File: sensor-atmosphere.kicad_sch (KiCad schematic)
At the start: 16 parts, among them J4 STEMMA_I2C_QT, J5 Conn_01x07, J6 STEMMA_I2C_QT, Q2 BSS138BKS,115, U6 XC6210B332MR-G, U7 BME688

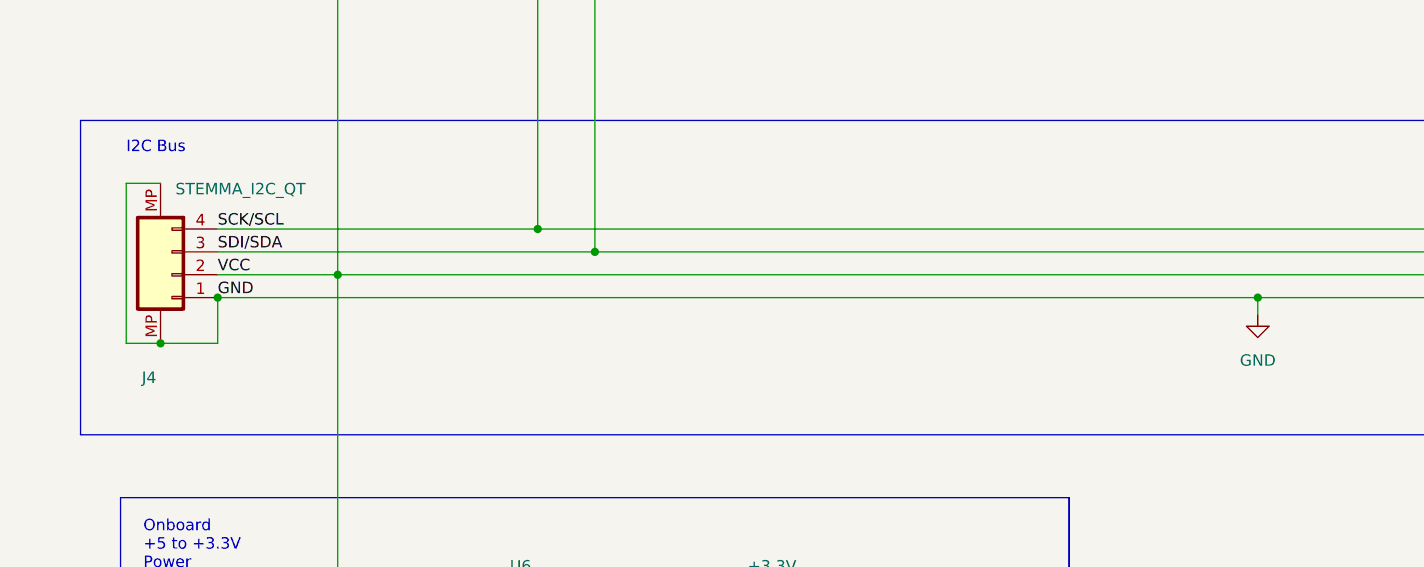
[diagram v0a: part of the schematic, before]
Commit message: Adding I2C bus to circuit
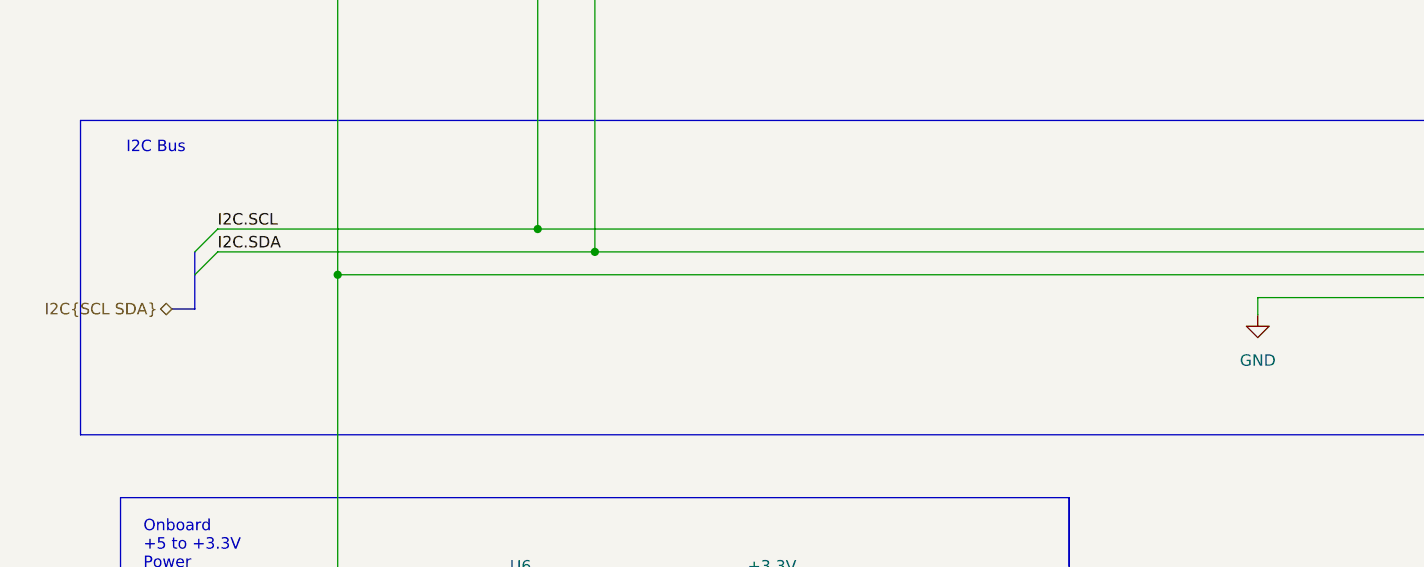
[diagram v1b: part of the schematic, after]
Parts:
- removed J4: STEMMA_I2C_QT, Connector_JST:JST_SH_SM04B-SRSS-TB_1x04-1MP_P1.00mm_Horizontal, symbol Lab_4:STEMMA_I2C_QT
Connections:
- net SCK/SCL renamed I2C.SCL
- net SDI/SDA renamed I2C.SDA
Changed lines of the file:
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@@
-	)
-	(junction
-		(at 40.64 119.38)
-		(diameter 0)
-		(color 0 0 0 0)
 	)
 	(junction
@@
 	)
 	(junction
-		(at 156.21 119.38)
-		(diameter 0)
-		(color 0 0 0 0)
-	)
-	(junction
 		(at 143.51 33.655)
 		(diameter 0)
@@
 	(junction
 		(at 66.675 154.305)
-		(diameter 0)
-		(color 0 0 0 0)
-	)
-	(junction
-		(at 34.29 124.46)
 		(diameter 0)
 		(color 0 0 0 0)
@@
 		(at 81.915 156.845)
 	)
+	(bus_entry
+		(at 40.64 114.3)
+		(size -2.54 2.54)
+		(stroke
+			(width 0)
+			(type default)
+		)
+	)
+	(bus_entry
+		(at 40.64 111.76)
+		(size -2.54 2.54)
+		(stroke
+			(width 0)
+			(type default)
+		)
+	)
 	(wire
 		(pts
@@
 		)
 	)
-	(wire
-		(pts
-			(xy 30.48 124.46) (xy 34.29 124.46)
-		)
-		(stroke
-			(width 0)
-			(type default)
-		)
-	)
 	(polyline
 		(pts
@@
 	(wire
 		(pts
-			(xy 30.48 106.68) (xy 34.29 106.68)
-		)
-		(stroke
-			(width 0)
-			(type default)
-		)
-	)
-	(wire
-		(pts
-			(xy 40.64 119.38) (xy 156.21 119.38)
-		)
-		(stroke
-			(width 0)
-			(type default)
-		)
-	)
-	(wire
-		(pts
 			(xy 102.235 164.465) (xy 90.17 164.465)
 		)
@@
 	(wire
 		(pts
-			(xy 34.29 124.46) (xy 40.64 124.46)
-		)
-		(stroke
-			(width 0)
-			(type default)
-		)
-	)
-	(wire
-		(pts
 			(xy 59.69 53.34) (xy 59.69 59.055)
 		)
@@
 		)
 	)
-	(wire
-		(pts
-			(xy 40.64 116.84) (xy 53.975 116.84)
+	(bus
+		(pts
+			(xy 35.56 120.65) (xy 38.1 120.65)
 		)
 		(stroke
@@
 	(wire
 		(pts
-			(xy 30.48 106.68) (xy 30.48 124.46)
-		)
-		(stroke
-			(width 0)
-			(type default)
-		)
-	)
-	(wire
-		(pts
 			(xy 238.76 75.565) (xy 236.22 75.565)
 		)
@@
 		)
 	)
+	(bus
+		(pts
+			(xy 38.1 114.3) (xy 38.1 116.84)
+		)
+		(stroke
+			(width 0)
+			(type default)
+		)
+	)
 	(wire
 		(pts
@@
 		)
 	)
+	(bus
+		(pts
+			(xy 38.1 116.84) (xy 38.1 120.65)
+		)
+		(stroke
+			(width 0)
+			(type default)
+		)
+	)
 	(wire
 		(pts
@@
 		(pts
 			(xy 113.03 46.355) (xy 113.03 62.865)
-		)
-		(stroke
-			(width 0)
-			(type default)
-		)
-	)
-	(wire
-		(pts
-			(xy 40.64 119.38) (xy 40.64 124.46)
 		)
 		(stroke
@@
 		)
 	)
-	(label "SCK{slash}SCL"
+	(label "I2C.SCL"
 		(at 40.64 111.76 0)
 		(fields_autoplaced yes)
@@
 		)
 	)
-	(label "VCC"
-		(at 40.64 116.84 0)
-		(fields_autoplaced yes)
-		(effects
-			(font
-				(size 1.27 1.27)
-			)
-			(justify left bottom)
-		)
-	)
-	(label "GND"
-		(at 40.64 119.38 0)
-		(fields_autoplaced yes)
-		(effects
-			(font
-				(size 1.27 1.27)
-			)
-			(justify left bottom)
-		)
-	)
 	(label "SDI_3V"
 		(at 215.9 62.865 0)
@@
 		)
 	)
-	(label "SDI{slash}SDA"
+	(label "I2C.SDA"
 		(at 40.64 114.3 0)
 		(fields_autoplaced yes)
@@
 			)
 			(justify left bottom)
+		)
+	)
+	(hierarchical_label "I2C{SCL SDA}"
+		(shape bidirectional)
+		(at 35.56 120.65 180)
+		(fields_autoplaced yes)
+		(effects
+			(font
+				(size 1.27 1.27)
+			)
+			(justify right)
 		)
 	)
@@
 					(unit 1)
 				)
-			)
-		)
-	)
-	(symbol
-		(lib_name "STEMMA_I2C_QT_1")
-		(lib_id "Lab_4:STEMMA_I2C_QT")
-		(at 35.56 116.84 180)
-		(unit 1)
-		(exclude_from_sim no)
-		(in_bom yes)
-		(on_board yes)
-		(dnp no)
-		(property "Reference" "J4"
-			(at 33.02 128.27 0)
-			(effects
-				(font
-					(size 1.27 1.27)
-				)
-			)
-		)
-		(property "Value" "STEMMA_I2C_QT"
-			(at 43.18 107.315 0)
-			(effects
-				(font
-					(size 1.27 1.27)
-				)
-			)
-		)
-		(property "Footprint" "Connector_JST:JST_SH_SM04B-SRSS-TB_1x04-1MP_P1.00mm_Horizontal"
-			(at 35.56 116.84 0)
-			(effects
-				(font
-					(size 1.27 1.27)
-				)
-				(hide yes)
-			)
-		)
-		(property "Datasheet" "https://www.jst-mfg.com/product/pdf/eng/eSH.pdf"
-			(at 35.56 116.84 0)
-			(effects
-				(font
-					(size 1.27 1.27)
-				)
-				(hide yes)
-			)
-		)
-		(property "Description" "Connector Header Surface Mount, Right Angle 4 position 0.039\" (1.00mm)"
-			(at 35.56 116.84 0)
-			(effects
-				(font
-					(size 1.27 1.27)
-				)
-				(hide yes)
-			)
-		)
-		(property "Vendor" "DigiKey"
-			(at 35.56 116.84 0)
-			(effects
-				(font
-					(size 1.27 1.27)
-				)
-				(hide yes)
-			)
-		)
-		(property "Vendor P/N" "455-1804-1-ND "
-			(at 35.56 116.84 0)
-			(effects
-				(font
-					(size 1.27 1.27)
-				)
-				(hide yes)
-			)
-		)
-		(property "Mfr" "JST Sales America Inc."
-			(at 35.56 116.84 0)
-			(effects
-				(font
-					(size 1.27 1.27)
-				)
-				(hide yes)
-			)
-		)
-		(property "Mfr P/N" "SM04B-SRSS-TB"
-			(at 35.56 116.84 0)
-			(effects
-				(font
-					(size 1.27 1.27)
-				)
-				(hide yes)
-			)
-		)
-		(property "Supplier 1" ""
-			(at 35.56 116.84 0)
-			(effects
-				(font
-					(size 1.27 1.27)
-				)
-				(hide yes)
-			)
-		)
-		(property "Supplier 1 P/N" ""
-			(at 35.56 116.84 0)
-			(effects
-				(font
-					(size 1.27 1.27)
-				)
-				(hide yes)
-			)
-		)
-		(property "Supplier 2" ""
-			(at 35.56 116.84 0)
-			(effects
-				(font
-					(size 1.27 1.27)
-				)
-				(hide yes)
-			)
-		)
-		(property "Supplier 2 P/N" ""
-			(at 35.56 116.84 0)
-			(effects
-				(font
-					(size 1.27 1.27)
-				)
-				(hide yes)
-			)
-		)
-		(pin "MP"
-		)
-		(pin "MP"
-		)
-		(pin "1"
-		)
-		(pin "2"
-		)
-		(pin "3"
-		)
-		(pin "4"
-		)
-		(instances
-			(project "roamer"
-				(path "/1c59de6a-87fe-4223-8898-4b0383164a31/10ed27ff-b06a-41c0-90a7-6ef09f5e2ce1"
-					(reference "J4")
-					(unit 1)
-				)

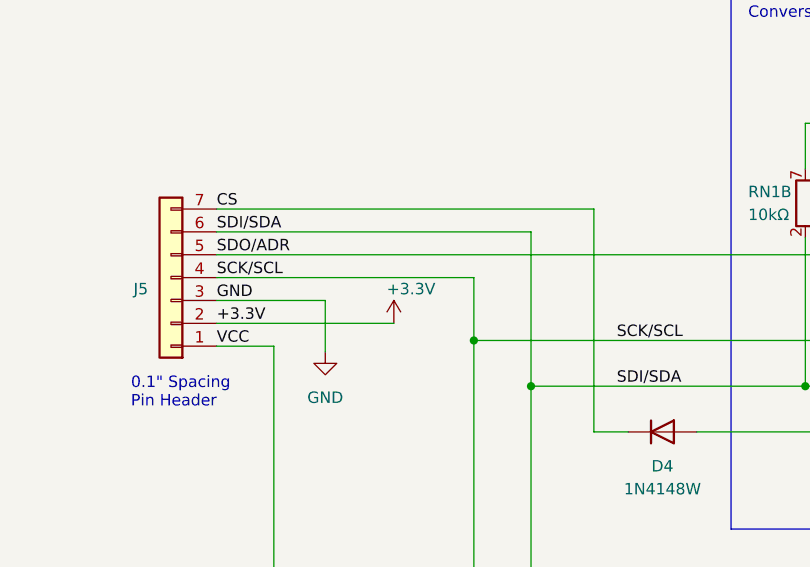
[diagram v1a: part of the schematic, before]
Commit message: Adding symbols information
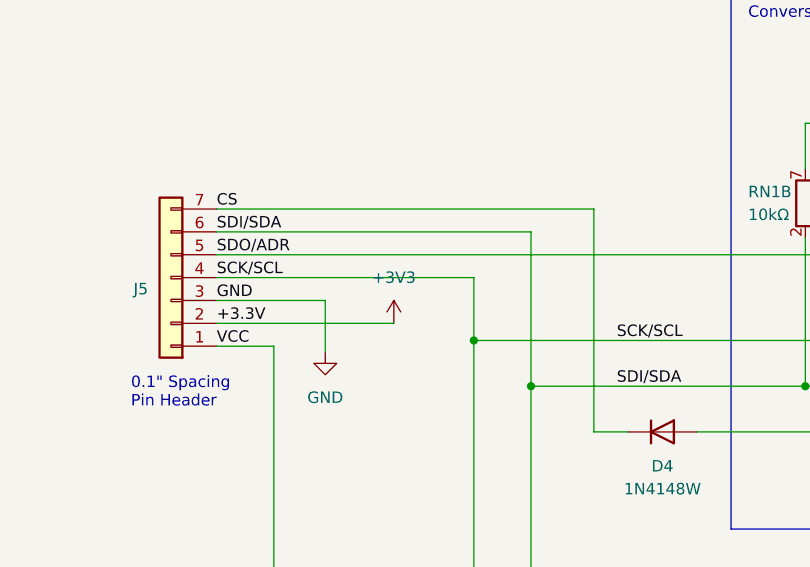
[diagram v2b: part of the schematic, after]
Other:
- company: (none) -> catbranchman
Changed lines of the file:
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@@
 	(generator_version "8.0")
 	(paper "A4")
+	(title_block
+		(company "catbranchman")
+		(comment 1 "Electrical Engineering Department")
+		(comment 2 "EE 156 / Stanford University")
+		(comment 3 "Flight Club, W6YX, Endurance")
+	)
 	(junction
 		(at 238.76 45.085)
@@
 	)
 	(symbol
-		(lib_name "+3.3V_3")
-		(lib_id "power:+3.3V")
-		(at 67.31 55.88 0)
-		(unit 1)
-		(exclude_from_sim no)
-		(in_bom yes)
-		(on_board yes)
-		(dnp no)
-		(property "Reference" "#PWR042"
-			(at 67.31 59.69 0)
-			(effects
-				(font
-					(size 1.27 1.27)
-				)
-				(hide yes)
-			)
-		)
-		(property "Value" "+3.3V"
-			(at 69.215 52.07 0)
-			(effects
-				(font
-					(size 1.27 1.27)
-				)
-			)
-		)
-		(property "Footprint" ""
-			(at 67.31 55.88 0)
-			(effects
-				(font
-					(size 1.27 1.27)
-				)
-				(hide yes)
-			)
-		)
-		(property "Datasheet" ""
-			(at 67.31 55.88 0)
-			(effects
-				(font
-					(size 1.27 1.27)
-				)
-				(hide yes)
-			)
-		)
-		(property "Description" ""
-			(at 67.31 55.88 0)
-			(effects
-				(font
-					(size 1.27 1.27)
-				)
-				(hide yes)
-			)
-		)
-		(property "Mfr" ""
-			(at 67.31 55.88 0)
-			(effects
-				(font
-					(size 1.27 1.27)
-				)
-				(hide yes)
-			)
-		)
-		(property "Mfr P/N" ""
-			(at 67.31 55.88 0)
-			(effects
-				(font
-					(size 1.27 1.27)
-				)
-				(hide yes)
-			)
-		)
-		(property "Supplier 1" ""
-			(at 67.31 55.88 0)
-			(effects
-				(font
-					(size 1.27 1.27)
-				)
-				(hide yes)
-			)
-		)
-		(property "Supplier 1 P/N" ""
-			(at 67.31 55.88 0)
-			(effects
-				(font
-					(size 1.27 1.27)
-				)
-				(hide yes)
-			)
-		)
-		(property "Supplier 2" ""
-			(at 67.31 55.88 0)
-			(effects
-				(font
-					(size 1.27 1.27)
-				)
-				(hide yes)
-			)
-		)
-		(property "Supplier 2 P/N" ""
-			(at 67.31 55.88 0)
-			(effects
-				(font
-					(size 1.27 1.27)
-				)
-				(hide yes)
-			)
-		)
-		(pin "1"
-		)
-		(instances
-			(project "roamer"
-				(path "/1c59de6a-87fe-4223-8898-4b0383164a31/10ed27ff-b06a-41c0-90a7-6ef09f5e2ce1"
-					(reference "#PWR042")
-					(unit 1)
-				)
-			)
-		)
-	)
-	(symbol
 		(lib_name "GND_6")
 		(lib_id "power:GND")
@@
 				)
 			)
+		)
+	)
+	(symbol
+		(lib_id "power:+3V3")
+		(at 67.31 55.88 0)
+		(unit 1)
+		(exclude_from_sim no)
+		(in_bom yes)
+		(on_board yes)
+		(dnp no)
+		(fields_autoplaced yes)
+		(property "Reference" "#PWR042"
+			(at 67.31 59.69 0)
+			(effects
+				(font
+					(size 1.27 1.27)
+				)
+				(hide yes)
+			)
+		)
+		(property "Value" "+3V3"
+			(at 67.31 50.8 0)
+			(effects
+				(font
+					(size 1.27 1.27)
+				)
+			)
+		)
+		(property "Footprint" ""
+			(at 67.31 55.88 0)
+			(effects
+				(font
+					(size 1.27 1.27)
+				)
+				(hide yes)
+			)
+		)
+		(property "Datasheet" ""
+			(at 67.31 55.88 0)
+			(effects
+				(font
+					(size 1.27 1.27)
+				)
+				(hide yes)
+			)
+		)
+		(property "Description" "Power symbol creates a global label with name \"+3V3\""
+			(at 67.31 55.88 0)
+			(effects
+				(font
+					(size 1.27 1.27)
+				)
+				(hide yes)
+			)
+		)
+		(pin "1"
+		)
+		(instances
+			(project "roamer"
+				(path "/1c59de6a-87fe-4223-8898-4b0383164a31/10ed27ff-b06a-41c0-90a7-6ef09f5e2ce1"
+					(reference "#PWR042")
+					(unit 1)
+				)
+			)

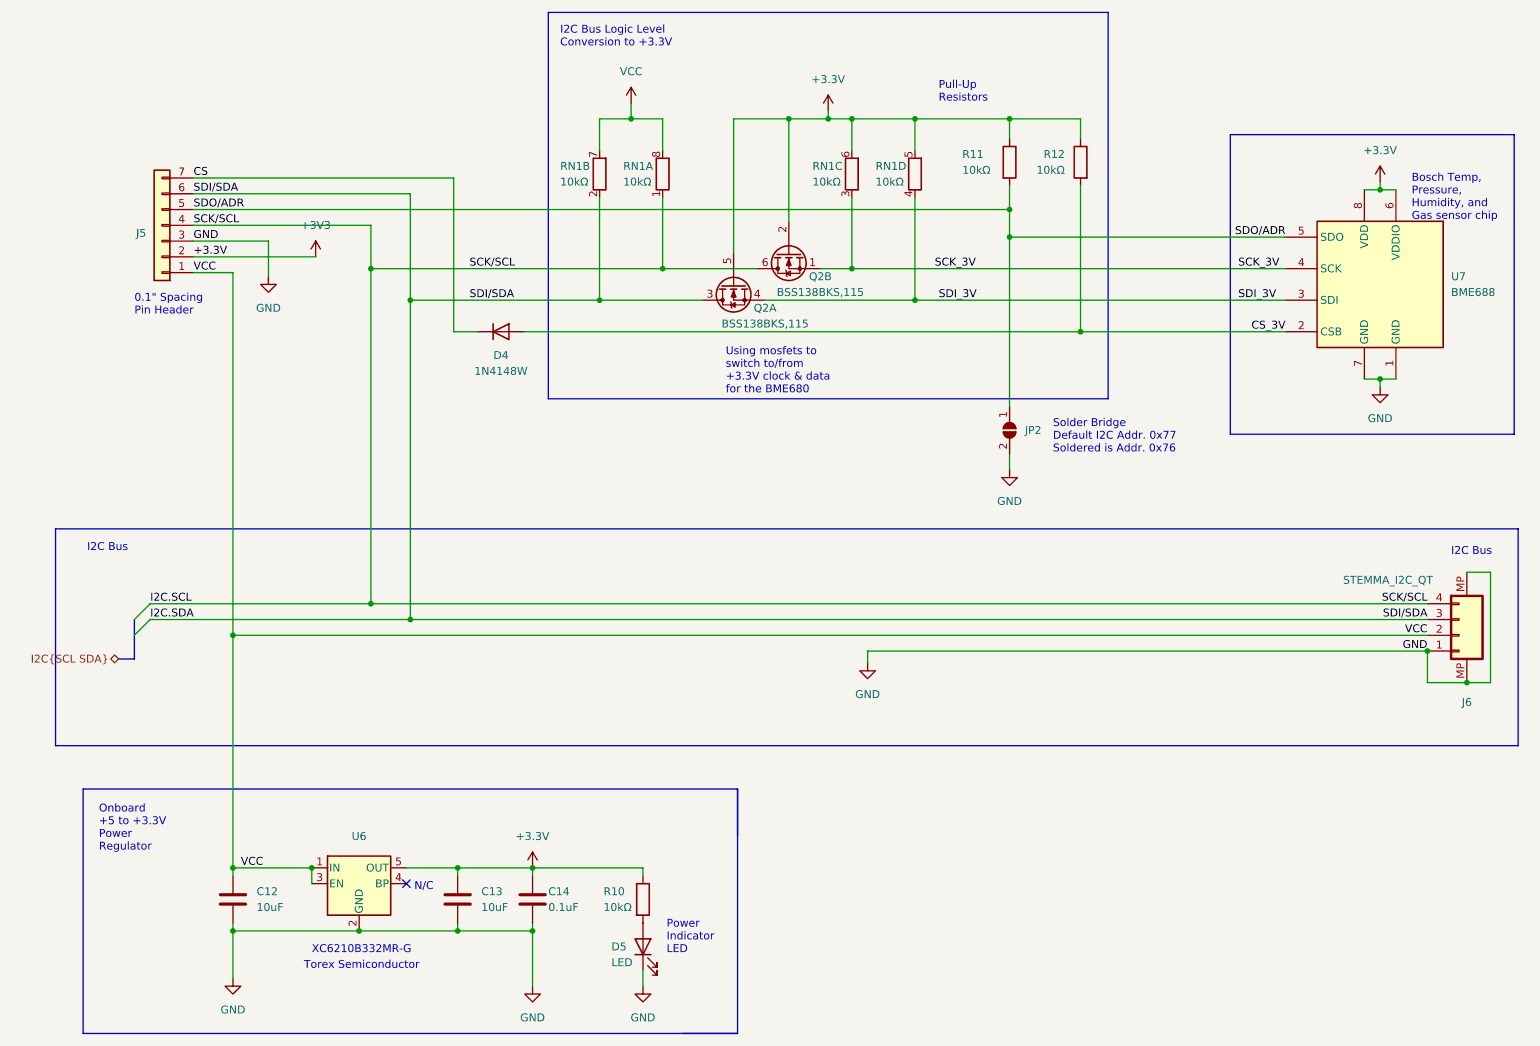
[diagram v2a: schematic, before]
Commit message: Adding rest of schematic
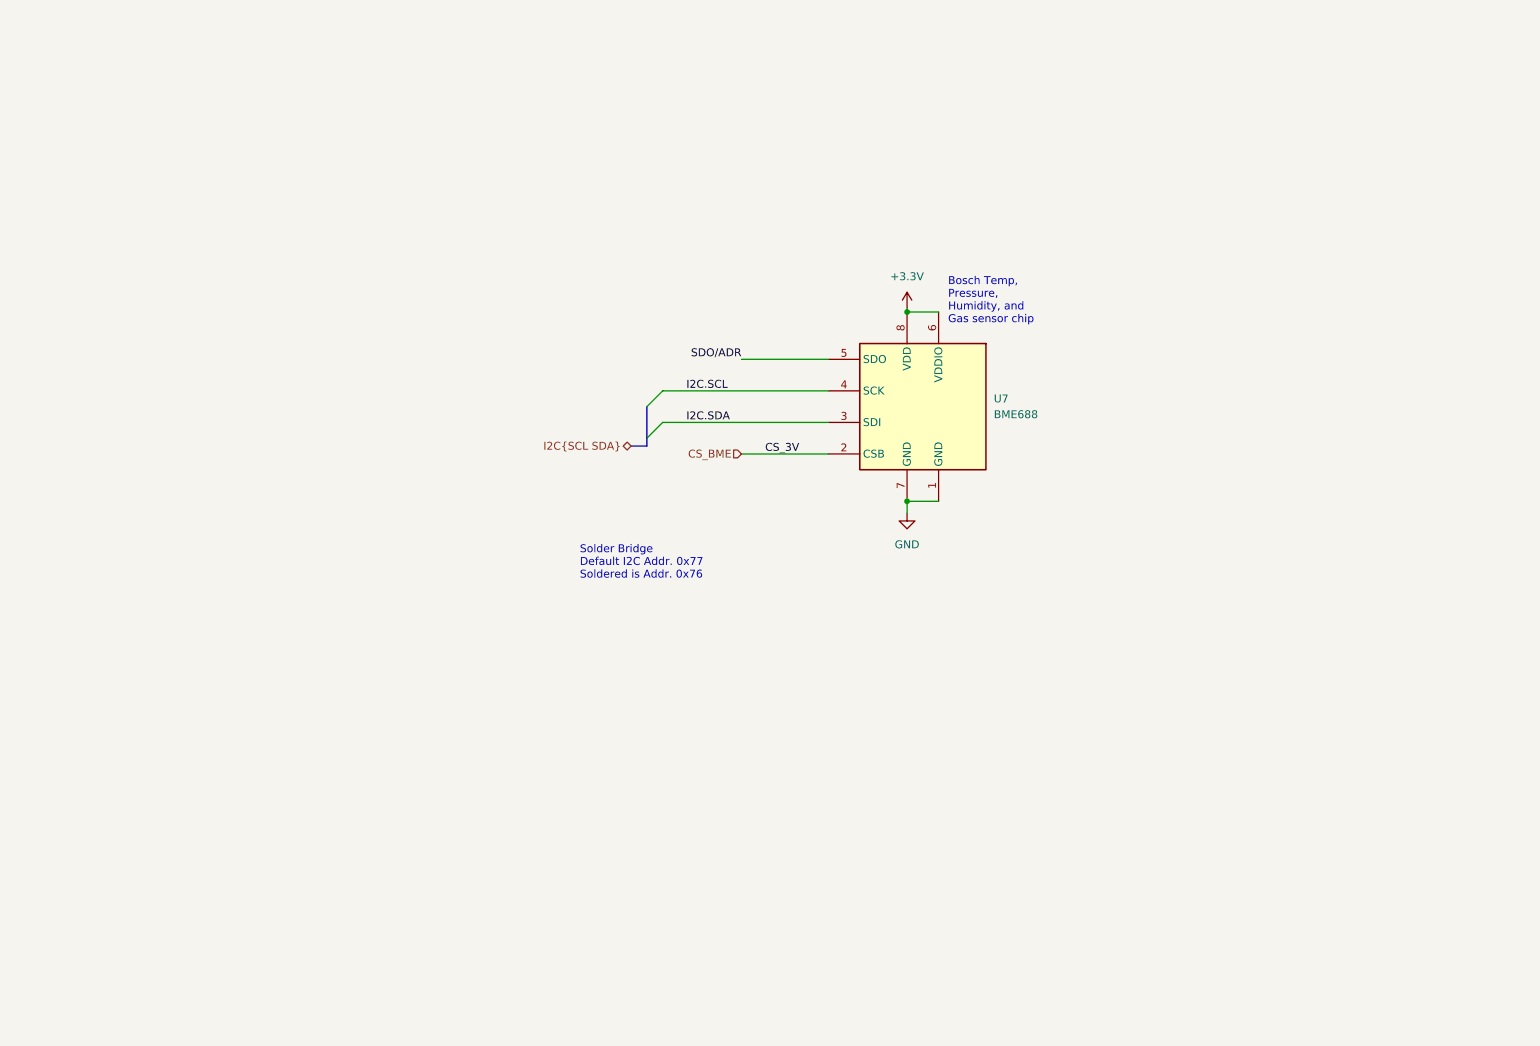
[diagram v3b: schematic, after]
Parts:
- removed C12, C13: 10uF, Capacitor_SMD:C_1206_3216Metric_Pad1.33x1.80mm_HandSolder, symbol Lab_4:C
- removed C14: 0.1uF, Capacitor_SMD:C_0805_2012Metric_Pad1.18x1.45mm_HandSolder, symbol Lab_4:C
- removed D4: 1N4148W, Diode_SMD:D_SOD-123, symbol Lab_4:1N4148W
- removed D5: LED, LED_SMD:LED_0805_2012Metric_Pad1.15x1.40mm_HandSolder, symbol Lab_4:LED
- removed J5: Conn_01x07, Connector_PinSocket_2.54mm:PinSocket_1x07_P2.54mm_Vertical, symbol Lab_4:Conn_01x07
- removed J6: STEMMA_I2C_QT, Connector_JST:JST_SH_SM04B-SRSS-TB_1x04-1MP_P1.00mm_Horizontal, symbol Lab_4:STEMMA_I2C_QT
- removed JP2: SolderJumper_2_Open, Jumper:SolderJumper-2_P1.3mm_Open_TrianglePad1.0x1.5mm, symbol Lab_4:SolderJumper_2_Open
- removed Q2: BSS138BKS,115, Package_TO_SOT_SMD:SOT-363_SC-70-6_Handsoldering, symbol Lab_4:2N7002D
- removed R10, R11, R12: 10kΩ, Resistor_SMD:R_0805_2012Metric_Pad1.20x1.40mm_HandSolder, symbol Lab_4:R
- removed RN1: 10kΩ, Resistor_SMD:R_Array_Convex_4x0612, symbol Lab_4:R_Pack04_Split
- removed U6: XC6210B332MR-G, Package_TO_SOT_SMD:SOT-23-5, symbol Lab_4:MIC5205-3.3YM5
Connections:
- net SCK_3V is gone; now on net I2C.SCL: U7.4 (SCK)
- net SDI_3V is gone; now on net I2C.SDA: U7.3 (SDI)
- net CS_3V renamed CS_BME
- no-connect marks 1 -> 0
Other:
- note removed: "0.1" Spacing Pin Header"
- note removed: "I2C Bus"
- note removed: "I2C Bus Logic Level Conversion to +3.3V"
- note removed: "N/C"
- note removed: "Onboard +5 to +3.3V Power Regulator"
- note removed: "Power Indicator LED"
- note removed: "Pull-Up Resistors"
- note removed: "Torex Semiconductor"
- note removed: "Using mosfets to switch to/from +3.3V clock & data for the BME680"
- note removed: "XC6210B332MR-G"
- moved on the sheet: U7
